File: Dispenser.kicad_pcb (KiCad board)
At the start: 2 copper layers, 10 parts, among them P1 Conn_01x02, U1 TMC2208_SILENTSTEPSTICK

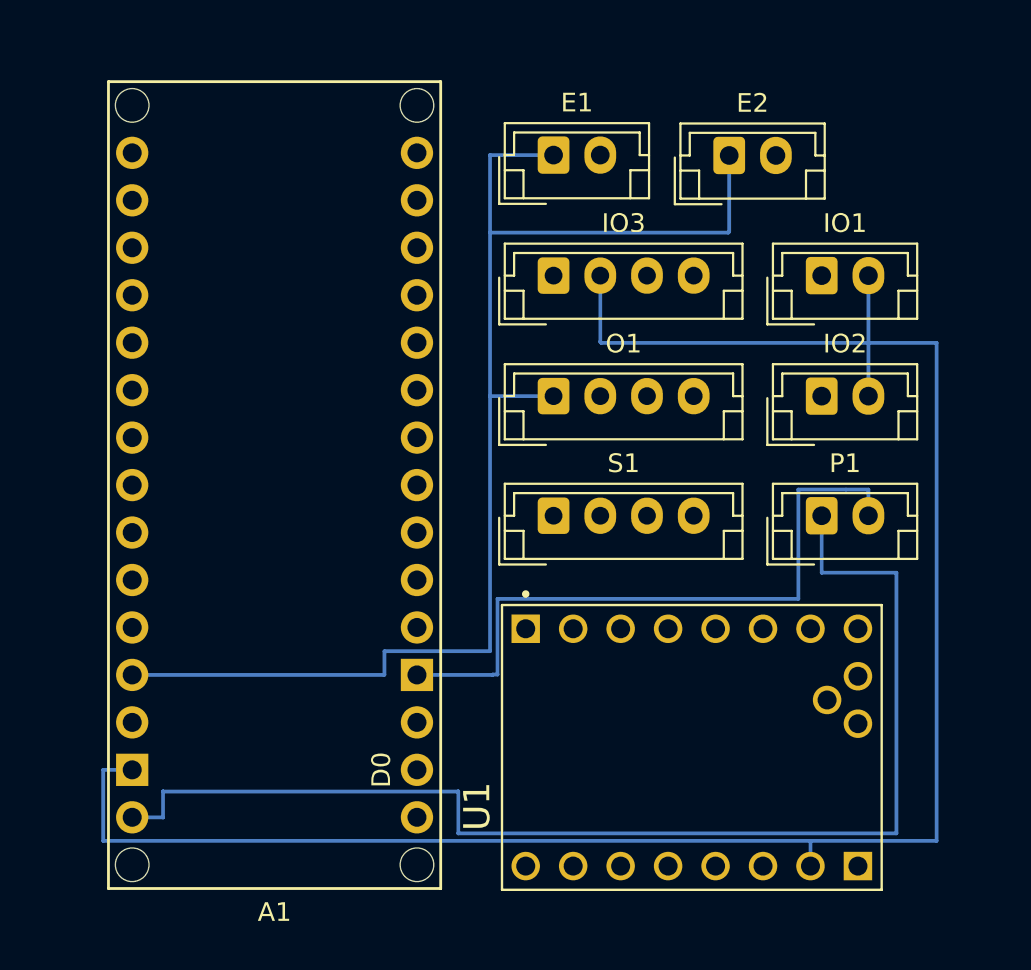
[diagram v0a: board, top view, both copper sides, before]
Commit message: Add Mounting Holes
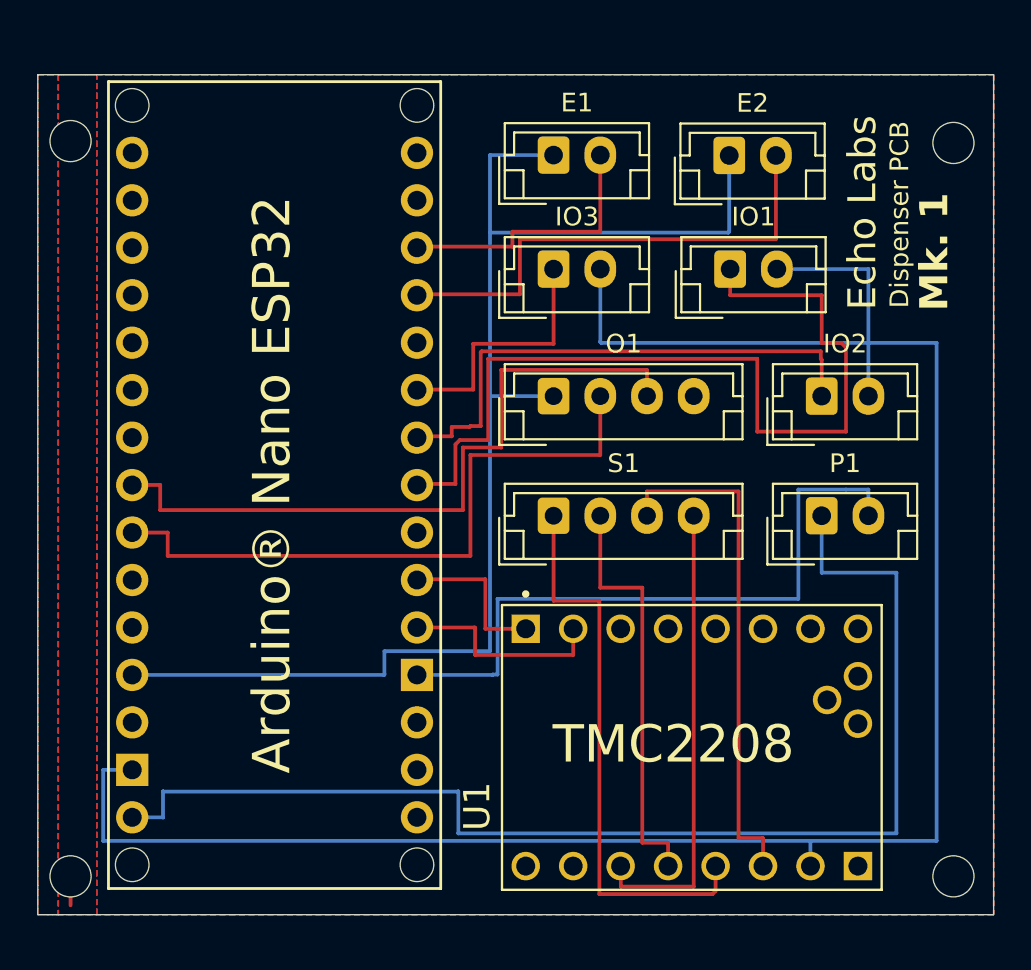
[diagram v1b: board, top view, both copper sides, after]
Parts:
- added H1: MountingHole, MountingHole:MountingHole_2.2mm_M2, F.Cu at (37.0, 27.2)
- added H2: MountingHole, MountingHole:MountingHole_2.2mm_M2, F.Cu at (37.0, 66.5)
- added H3: MountingHole, MountingHole:MountingHole_2.2mm_M2, F.Cu at (84.2, 27.3)
- added H3: MountingHole, MountingHole:MountingHole_2.2mm_M2, F.Cu at (84.2, 66.5)
- IO3: footprint Connector_JST:JST_EH_B4B-EH-A_1x04_P2.50mm_Vertical -> Connector_JST:JST_EH_B2B-EH-A_1x02_P2.50mm_Vertical
- moved IO1 4.91 mm to (72.2, 34.0)
- moved IO3 0.35 mm to (62.8, 34.0)
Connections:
- A1 pad D10: unconnected-(A1-PadD10) -> E1
- A1 pad D9: unconnected-(A1-PadD9) -> E2
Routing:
- net IO 1: track 0.00 -> 48.2 mm
- net SDA: track 0.00 -> 37.8 mm
- net SCL: track 0.00 -> 34.8 mm
- net A+: track 0.00 -> 30.3 mm
- net IO 2: track 0.00 -> 28.6 mm
- net A-: track 0.00 -> 27.6 mm
- net E2: track 0.00 -> 26.7 mm
- net B-: track 0.00 -> 24.9 mm
- net B+: track 0.00 -> 22.4 mm
- net E1: track 0.00 -> 14.7 mm
- net IO 3: track 0.00 -> 13.8 mm
- net DIR: track 0.00 -> 11.2 mm
- net STEP: track 0.00 -> 8.49 mm
- net GND1: track 141.4 -> 146.7 mm
- added copper zone on B.Cu, net (none)
- added copper zone on F.Cu, net (none)
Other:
- board outline added: 51.1 x 44.9 mm
- board text added: "Arduino® Nano ESP32"
- board text added: "Dispenser PCB"
- board text added: "Echo Labs"
- board text added: "Mk. 1"
- board text added: "TMC2208"
